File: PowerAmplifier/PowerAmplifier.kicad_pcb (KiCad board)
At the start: 4 copper layers, 121 x 40 mm, 153 parts, among them J1 A_SE, J10 AMP, J11 OSC, J12 12V, J13 VADJ, J14 I2C, J15 SWD, J2 AB_IN, J3 AB_BTL, J4 B_SE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

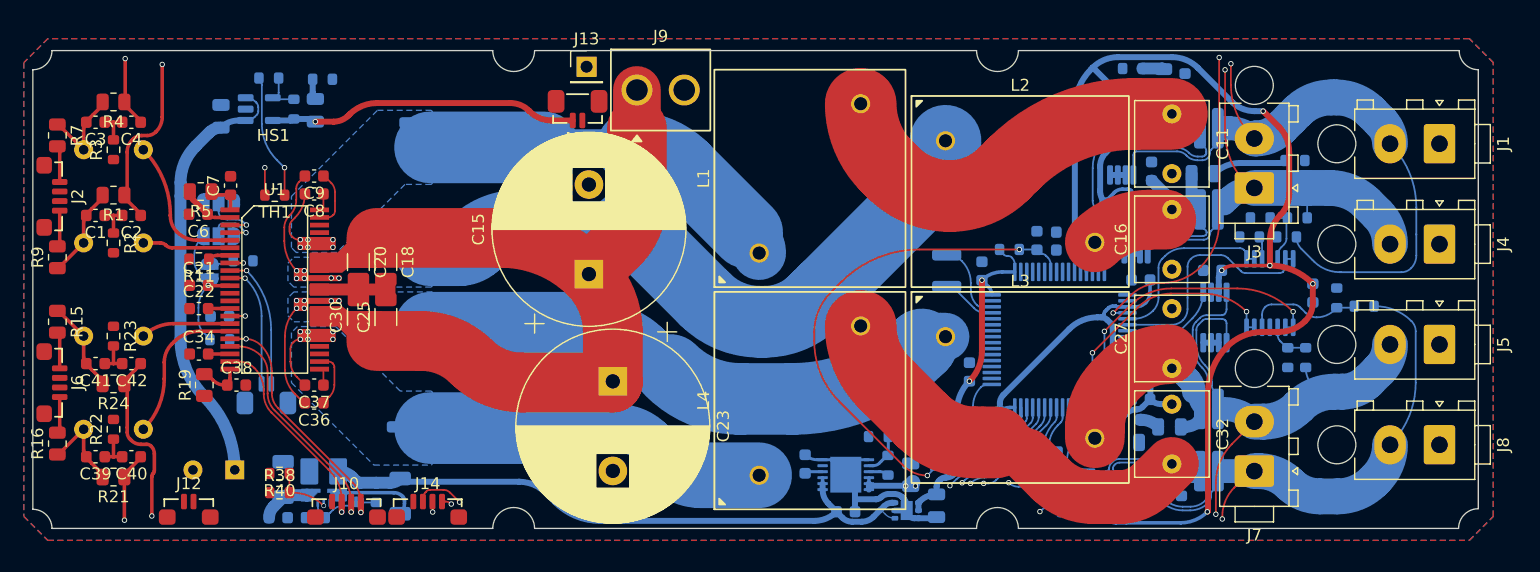
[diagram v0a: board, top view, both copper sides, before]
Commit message: PowerAmplifier initially complete, PowerAmpSupply progress
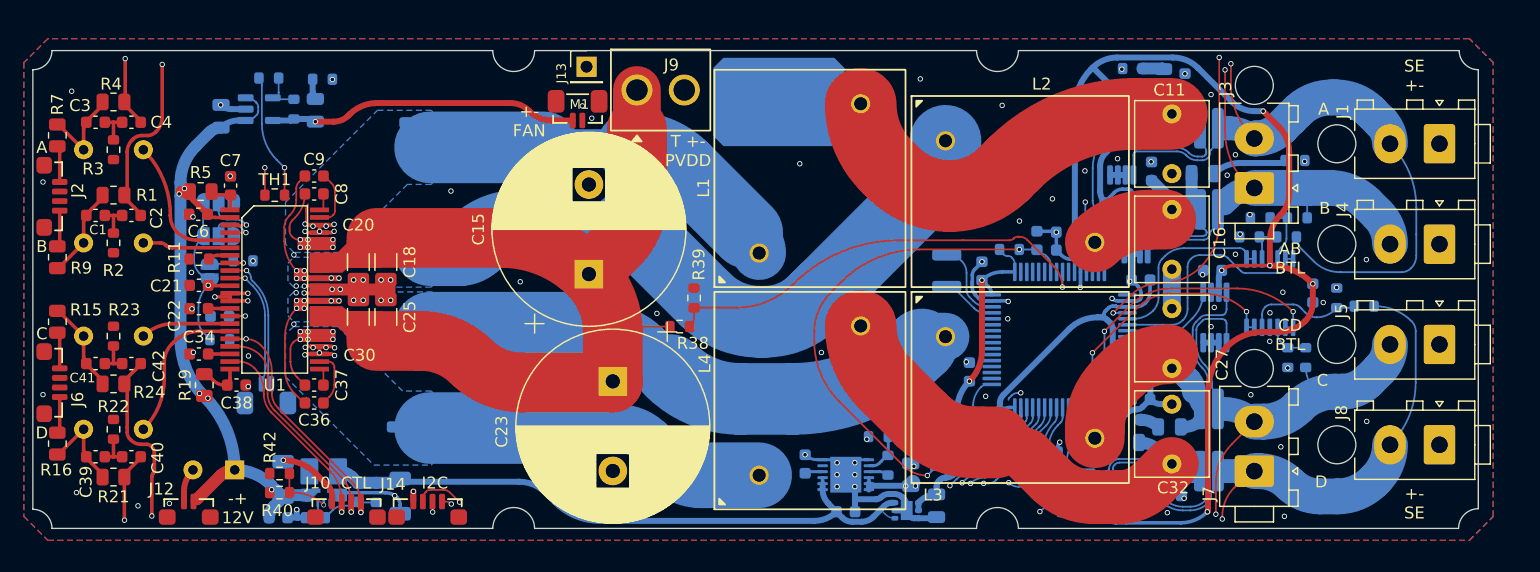
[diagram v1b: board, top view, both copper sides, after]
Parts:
- added R38: 200kΩ 0.1%, Resistor_SMD:R_0603_1608Metric, F.Cu at (143.9, 103.1)
- added R39: 11kΩ 0.1%, Resistor_SMD:R_0603_1608Metric, F.Cu at (145.1, 100.7)
- added REF**: BW_Logo_10x6.4mm, BW_Logo:BW_Logo_10x6.4mm, B.Cu at (152.2, 84.3)
- renumbered R38 to R40, R39 to R41, R40 to R42, R41 to R43, R42 to R44, R43 to R45
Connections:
- U8 pad 9: unconnected-(U8-PC1-Pad9) -> Net-(U8-PC1)
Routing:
- net GND: track 50.1 -> 111.2 mm, vias 1 -> 115
- net Net-(U8-PC1): track 0.00 -> 37.5 mm, vias 0 -> 1
- net +12V: track 45.2 -> 55.4 mm, vias 0 -> 5
- net PVDD: track 67.6 -> 72.5 mm
- net /Controller/D_SENSE+: track 52.2 -> 57.0 mm
- net Net-(C35-Pad2): track 0.00 -> 3.85 mm
- net /DVDD: track 11.9 -> 14.7 mm
- net Net-(U3A-+): track 1.89 -> 3.34 mm
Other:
- board text added: "+- FAN"
- board text added: "+- SE"
- board text added: "-+ 12V"
- board text added: "A"
- board text added: "AB BTL"
- board text added: "B"
- board text added: "C"
- board text added: "CD BTL"
- board text added: "CTL"
- board text added: "D"
- board text added: "DEBUG TX RX"
- board text added: "I2C"
- board text added: "M1"
- board text added: "M2"
- board text added: "Modular Audio Power Amplifier"
- board text added: "OSC -+"
- board text added: "SE +-"
- board text added: "SLAVE"
- board text added: "SWD"
- board text added: "T +- PVDD"

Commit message: PowerAmpSupply FET change and layout progress
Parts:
- HS1: value ATS-FPX035035035-90-C1-R0_NoMounts -> ATS-xPX035035035_NoMounts; footprint BW_PassiveMechanical:ATS-FPX035035035-90-C1-R0_NoMounts -> BW_PassiveMechanical:ATS-xPX035035035_NoMounts
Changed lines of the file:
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@@
 		)
 	)
-	(footprint "BW_PassiveMechanical:ATS-FPX035035035-90-C1-R0_NoMounts"
+	(footprint "BW_PassiveMechanical:ATS-xPX035035035_NoMounts"
 		(layer "F.Cu")
 		(at 109.875 100)
 		(property "Reference" "HS1"
+			(at 0 -12.9 0)
+			(layer "F.Fab")
+			(effects
+				(font
+					(size 1 1)
+					(thickness 0.15)
+				)
+			)
+		)
+		(property "Value" "ATS-xPX035035035_NoMounts"
 			(at 0 0 0)
 			(layer "F.Fab")
@@
 			)
 		)
-		(property "Value" "ATS-FPX035035035-90-C1-R0_NoMounts"
-			(at 0 0 0)
-			(layer "F.Fab")
-			(effects
-				(font
-					(size 1 1)
-					(thickness 0.15)
-				)
-			)
-		)
-		(property "Footprint" "BW_PassiveMechanical:ATS-FPX035035035-90-C1-R0_NoMounts"
+		(property "Footprint" "BW_PassiveMechanical:ATS-xPX035035035_NoMounts"
 			(at 0 0 0)
 			(layer "F.Fab")
@@
 			(layer "F.Fab")
 		)
-		(model "E:/Users/Alex/Documents/KiCad/8.0/3dmodels/ATS-FPX-90-CX-R0_FUSED.STEP"
-			(opacity 0.6000)
-			(offset
-				(xyz 0 0 3)
-			)
-			(scale
-				(xyz 1 1 1)
-			)
-			(rotate
-				(xyz -90 0 0)
-			)
-		)
 	)

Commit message: PowerAmp+Supply additions
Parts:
- R27: value 470Ω -> 0Ω
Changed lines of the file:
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@@
 			)
 		)
-		(property "Value" "470Ω"
+		(property "Value" "0Ω"
 			(at 0 -1.43 0)
 			(layer "B.Fab")
